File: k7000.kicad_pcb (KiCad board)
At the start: 2 copper layers, 61 x 43.2 mm, 7 parts, among them J1 Conn_01x13

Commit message: fixed issues
added silkscreen
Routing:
- net Net-(RV2-Pad1): track 0.00 -> 2.80 mm
- net Net-(RV6-Pad1): track 35.1 -> 35.8 mm
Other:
- board text added: "10k"
- board text added: "200Ω"
- board text added: "25k"
- board text added: "2k"
- board text added: "500k"
- board text added: "500Ω"
- board text added: "BLK LEVEL"
- board text added: "CONTRAST"
- board text added: "H-POS"
- board text added: "If you paid for files,you got scammed! Files free at github.com/wrennnnnn/K7000-remote"
- board text added: "V-HOLD"
- board text added: "V-POS"
- board text added: "V-SIZE"
- board text removed: "If you paid for files, you got scammed! Files free at github.com/wrennnnnn/K7000-remote"

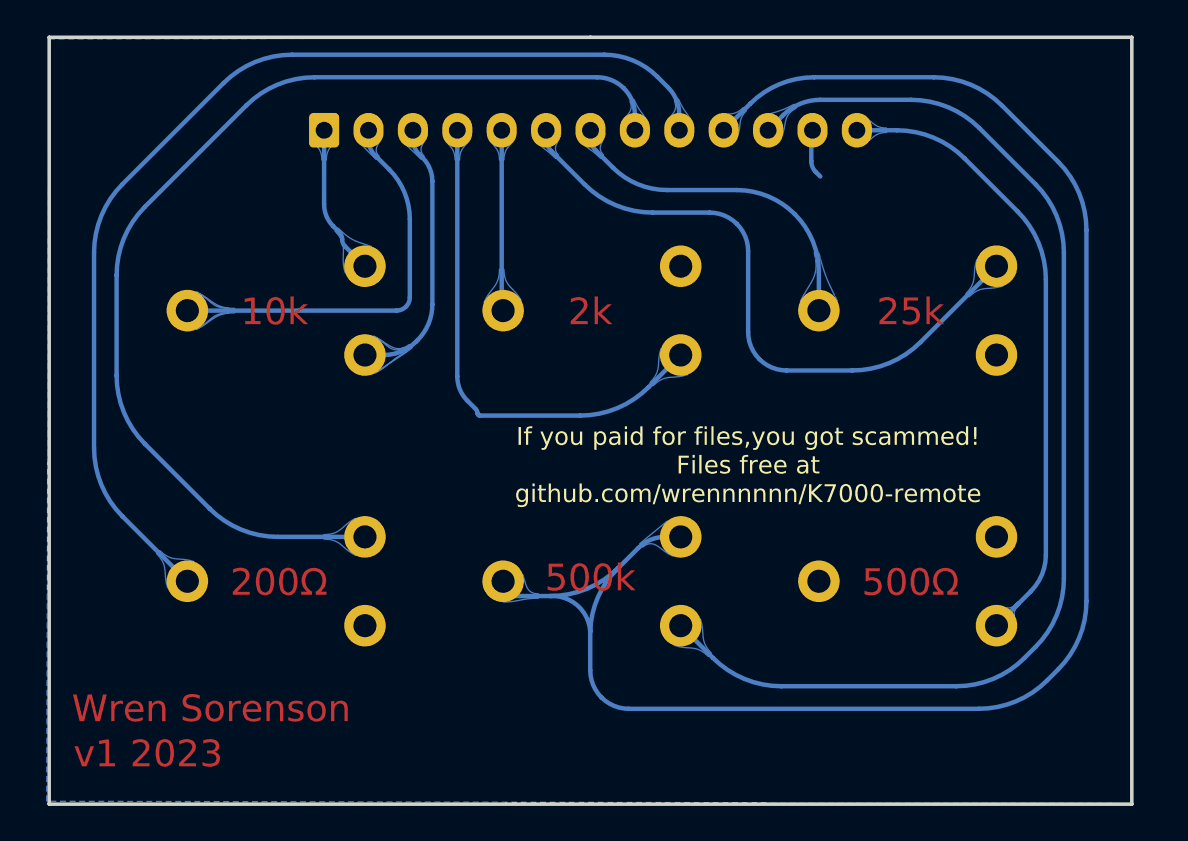
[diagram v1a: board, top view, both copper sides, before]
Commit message: remade files
added chamfer, flipped copper layer, added JLC watermark option for under the connector
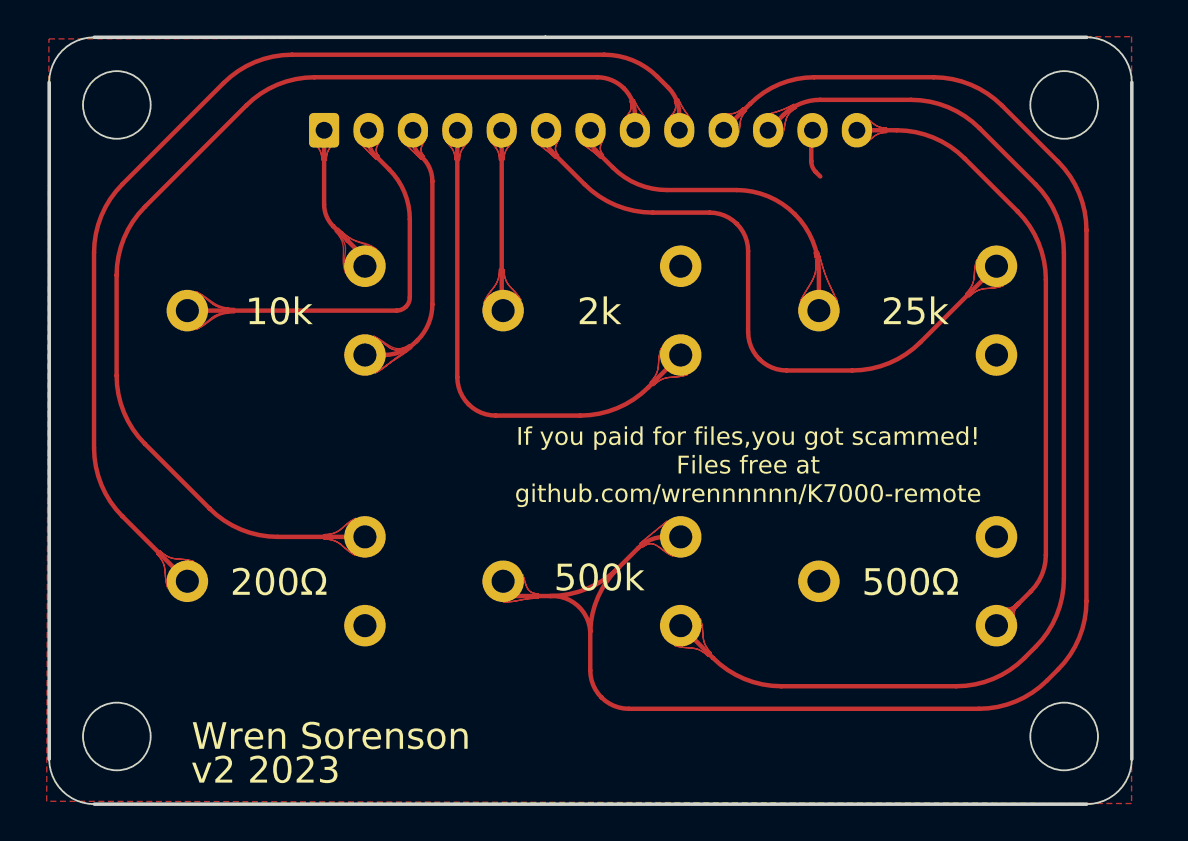
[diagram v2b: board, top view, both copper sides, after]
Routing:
- added copper zone on F.Cu, net Net-(RV2-Pad1)
- removed copper zone on B.Cu, net Net-(RV2-Pad1)
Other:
- outline, holes or cut-outs redrawn
- board text added: "JLCJLCJLCJLC"
- board text added: "v2 2023"
- board text removed: "v1 2023"
